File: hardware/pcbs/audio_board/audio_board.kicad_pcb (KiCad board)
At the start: 4 copper layers, 152 x 61.5 mm, 147 parts, among them J1 NC3FAH1, J10 DECT, J11 Conn_01x08, J2 NC3FAH1, J3 NC3FAH1, J4 NC3MAH, J5 NC3MAH, J6 AudioJack3, J7 Stereo Line-in, J8 I2C, Q1 2N7002, Q2 SI2309CDS-T1-GE3, Q3 2N7002, Q4 SI2309CDS-T1-GE3, Q5 2N7002, Q6 SI2309CDS-T1-GE3, Q7 S8050, U1 TAD5242, U2 TAD5242, U3 TAA3040, U5 LP5907MFX-3.3, U6 LM5158

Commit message: final touches to libraries
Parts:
- removed the U2 at (91.5, 120.5)
- added R7: 47, Resistor_SMD:R_0805_2012Metric, F.Cu at (174.2, 18.3)
- added R8: 47, Resistor_SMD:R_0805_2012Metric, F.Cu at (174.2, 21.2)
- added U5: TAD5242, ics:Texas_RGE0024R_VQFN-24-1EP_4x4mm_P0.5mm_EP2.1x2.1mm, F.Cu at (181.6, 28.3)
- J2: renamed from J11; footprint Library:mta100_01x8_P2.54_647050-8 -> Connector_MTA-100:mta100_01x8_P2.54_647050-8
- J3: renamed from J4; footprint Library:Jack_XLR_Neutrik_NC3MAH_Horizontal -> conn:Jack_XLR_Neutrik_NC3MAH_Horizontal
- J5: footprint Library:Jack_XLR_Neutrik_NC3MAH_Horizontal -> conn:Jack_XLR_Neutrik_NC3MAH_Horizontal
- J6: renamed from J1; footprint Library:Jack_XLR_Neutrik_NC3FAH2-LR-DAE_Horizontal -> conn:Jack_XLR_Neutrik_NC3FAH2-LR-DAE_Horizontal
- J7: renamed from J2; footprint Library:Jack_XLR_Neutrik_NC3FAH2-LR-DAE_Horizontal -> conn:Jack_XLR_Neutrik_NC3FAH2-LR-DAE_Horizontal
- J8: renamed from J3; footprint Library:Jack_XLR_Neutrik_NC3FAH2-LR-DAE_Horizontal -> conn:Jack_XLR_Neutrik_NC3FAH2-LR-DAE_Horizontal
- J9: renamed from J10; footprint Library:DectModule -> extra:DectModule
- U1: value TAD5242 -> ~; footprint Library:Texas_RGE0024R_VQFN-24-1EP_4x4mm_P0.5mm_EP2.1x2.1mm -> extra:Teensy41
- U3: value TAA3040 -> LM5158; footprint Package_DFN_QFN:WQFN-24-1EP_4x4mm_P0.5mm_EP2.6x2.6mm -> Package_DFN_QFN:WQFN-16-1EP_3x3mm_P0.5mm_EP1.68x1.68mm_ThermalVias
- U4: value ~ -> TAD5242; footprint Library:Teensy41 -> ics:Texas_RGE0024R_VQFN-24-1EP_4x4mm_P0.5mm_EP2.1x2.1mm
- U6: value LM5158 -> TAA3040; footprint Package_DFN_QFN:WQFN-16-1EP_3x3mm_P0.5mm_EP1.68x1.68mm_ThermalVias -> Package_DFN_QFN:WQFN-24-1EP_4x4mm_P0.5mm_EP2.6x2.6mm
- moved U6 127.5 mm to (181.9, 20.0)
- moved U1 112.0 mm to (163.1, 25.7), turned to 0 degrees
- moved U4 79.8 mm to (181.6, 36.6), turned to 0 degrees
- moved U3 69.4 mm to (181.4, 44.4)
- renumbered C29 to C1, C50 to C10, C51 to C11, C52 to C12, C9 to C13, C7 to C14, C11 to C15, C3 to C16, C1 to C17, C13 to C18, C5 to C19, C30 to C2, C2 to C20, C4 to C21, C6 to C22, C8 to C23, C10 to C24, C12 to C25, C14 to C26, C53 to C27, C15 to C28, C16 to C29, C37 to C3, C17 to C30, C18 to C31, C19 to C32, C20 to C33, C21 to C34, C22 to C35, C23 to C36, C24 to C37, C25 to C38, C26 to C39, C38 to C4, C27 to C40, C28 to C41, C31 to C42, C32 to C43, C33 to C44, C34 to C45, C35 to C46, C36 to C47, C41 to C48, C42 to C49, C39 to C5, C43 to C50, C44 to C51, C45 to C52, C46 to C53, C40 to C6, C47 to C7, C48 to C8, C49 to C9, D4 to D1, D5 to D2, D6 to D3, D1 to D4, D2 to D5, D3 to D6, H3 to H2, H2 to H3, J8 to J1, J7 to J10, J6 to J4, L7 to L1, L8 to L2, L9 to L3, L1 to L4, L2 to L5, L3 to L6, L4 to L7, L5 to L8, L6 to L9, Q7 to Q1, Q1 to Q2, Q2 to Q3, Q3 to Q4, Q4 to Q5, Q5 to Q6, Q6 to Q7, R11 to R1, R48 to R10, R49 to R11, R50 to R12, R51 to R13, R52 to R14, R1 to R15, R2 to R16, R3 to R17, R4 to R18, R5 to R19, R12 to R2, R7 to R20, R8 to R21, R9 to R22, R10 to R23, R15 to R24, R16 to R25, R17 to R26, R18 to R27, R19 to R28, R20 to R29, R13 to R3, R21 to R30, R22 to R31, R23 to R32, R24 to R33, R25 to R34, R26 to R35, R27 to R36, R29 to R37, R30 to R38, R31 to R39, R14 to R4, R32 to R40, R35 to R41, R36 to R42, R37 to R43, R38 to R44, R39 to R45, R40 to R46, R41 to R47, R42 to R48, R43 to R49, R71 to R5, R44 to R50, R45 to R51, R46 to R52, R6 to R53, R28 to R54, R72 to R6, R47 to R9, U5 to U2
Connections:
- C11 pad 1: Net-(U6-COMP) -> Net-(U3-COMP)
- C16 pad 1: Net-(U1-DREG) -> Net-(U4-DREG)
- C17 pad 1: Net-(U1-VREF) -> Net-(U4-VREF)
- C19 pad 1: Net-(U1-DREG) -> Net-(U4-DREG)
- C27 pad 1: Net-(U3-VREF) -> Net-(U6-VREF)
- C28 pad 1: Net-(U3-AREG) -> Net-(U6-AREG)
- C29 pad 1: Net-(U3-AREG) -> Net-(U6-AREG)
- C34 pad 1: Net-(U3-DREG) -> Net-(U6-DREG)
- C35 pad 1: Net-(U3-DREG) -> Net-(U6-DREG)
- C7 pad 1: Net-(U6-VCC) -> Net-(U3-VCC)
- C8 pad 1: Net-(U6-SS) -> Net-(U3-SS)
- J4 pad S: /HP_GND -> Net-(J4-PadS)
- R10 pad 2: Net-(U6-RT) -> Net-(U3-RT)
- R11 pad 2: Net-(U6-MODE) -> Net-(U3-MODE)
- R12 pad 1: Net-(U6-FB) -> Net-(U3-FB)
- R13 pad 2: Net-(U6-FB) -> Net-(U3-FB)
- R14 pad 2: Net-(U6-COMP) -> Net-(U3-COMP)
- R15 pad 1: Net-(U1-MD0) -> Net-(U4-MD0)
- U1 pad 1: Net-(U1-DREG) -> unconnected-(U1-Pad1)
- U1 pad 10: GND -> /CS_RIGHT
- U1 pad 11: unconnected-(U1-GPO-Pad11) -> /MOSI
- U1 pad 12: GND -> /DC
- U1 pad 13: Net-(U1-MD0) -> /SCK
- U1 pad 14: GND -> /DECT_TX
- U1 pad 15: GND -> /DECT_RX
- U1 pad 16: GND -> /SCL1
- U1 pad 17: GND -> /SDA1
- U1 pad 18: GND -> /SDA
- U1 pad 19: /DAC 1/OUTA- -> /SCL
- U1 pad 2: /I2S1_BCLK -> /I2S2_TX
- U1 pad 20: /DAC 1/OUTA+ -> /I2S1_LRCLK
- U1 pad 21: /DAC 1/OUTB+ -> /I2S1_BCLK
- U1 pad 22: /DAC 1/OUTB- -> unconnected-(U1-Pad22)
- U1 pad 23: +3.3VA -> /I2S1_MCLK
- U1 pad 24: Net-(U1-VREF) -> /RESET
- U1 pad 25: GND -> unconnected-(U1-Pad25)
- U1 pad 3: /I2S1_LRCLK -> /I2S2_FS
- U1 pad 4: /DAC 1/DOUT -> /I2S2_BCLK
- U1 pad 5: /I2S1_TX1 -> /I2S2_RX
- U1 pad 6: +3.3V -> /I2S1_RX2
- U1 pad 7: +3.3V -> /I2S1_TX1
- U1 pad 8: +3.3V -> /I2S1_RX1
- U1 pad 9: GND -> /CS_LEFT
- U3 pad 1: +3.3VA -> GND
- U3 pad 10: /ADC/IN3+ -> Net-(U3-SS)
- U3 pad 11: /ADC/IN3- -> Net-(U3-MODE)
- U3 pad 12: /ADC/IN4+ -> unconnected-(U3-NC-Pad12)
- U3 pad 13: GND -> /Power/SW
- U3 pad 14: +3.3V -> /Power/SW
- U3 pad 15: +3.3V -> unconnected-(U3-NC-Pad15)
- U3 pad 17: /SCL1 -> GND
- U3 pad 2: Net-(U3-AREG) -> Net-(U3-VCC)
- U3 pad 3: Net-(U3-VREF) -> +5V
- U3 pad 4: GND -> unconnected-(U3-PGOOD-Pad4)
- U3 pad 5: unconnected-(U3-MICBIAS-Pad5) -> Net-(U3-RT)
- U3 pad 6: /ADC/IN1+ -> +5V
- U3 pad 7: /ADC/IN1- -> GND
- U3 pad 8: /ADC/IN2+ -> Net-(U3-COMP)
- U3 pad 9: /ADC/IN2- -> Net-(U3-FB)
- U4 pad 1: unconnected-(U4-Pad1) -> Net-(U4-DREG)
- U4 pad 10: /CS_RIGHT -> GND
- U4 pad 11: /MOSI -> unconnected-(U4-GPO-Pad11)
- U4 pad 12: /DC -> GND
- U4 pad 13: /SCK -> Net-(U4-MD0)
- U4 pad 14: /DECT_TX -> GND
- U4 pad 15: /DECT_RX -> GND
- U4 pad 16: /SCL1 -> GND
- U4 pad 17: /SDA1 -> GND
- U4 pad 18: /SDA -> GND
- U4 pad 19: /SCL -> /DAC 1/OUTA-
- U4 pad 2: /I2S2_TX -> /I2S1_BCLK
- U4 pad 20: /I2S1_LRCLK -> /DAC 1/OUTA+
- U4 pad 21: /I2S1_BCLK -> /DAC 1/OUTB+
- U4 pad 22: unconnected-(U4-Pad22) -> /DAC 1/OUTB-
- U4 pad 23: /I2S1_MCLK -> +3.3VA
- U4 pad 24: /RESET -> Net-(U4-VREF)
- U4 pad 25: unconnected-(U4-Pad25) -> GND
- U4 pad 3: /I2S2_FS -> /I2S1_LRCLK
- U4 pad 4: /I2S2_BCLK -> /DAC 1/DOUT
- U4 pad 5: /I2S2_RX -> /I2S1_TX1
- U4 pad 6: /I2S1_RX2 -> +3.3V
- U4 pad 7: /I2S1_TX1 -> +3.3V
- U4 pad 8: /I2S1_RX1 -> +3.3V
- U4 pad 9: /CS_LEFT -> GND
- U6 pad 1: GND -> +3.3VA
- U6 pad 10: Net-(U6-SS) -> /ADC/IN3+
- U6 pad 11: Net-(U6-MODE) -> /ADC/IN3-
- U6 pad 12: unconnected-(U6-NC-Pad12) -> /ADC/IN4+
- U6 pad 13: /Power/SW -> GND
- U6 pad 14: /Power/SW -> +3.3V
- U6 pad 15: unconnected-(U6-NC-Pad15) -> +3.3V
- U6 pad 17: (no net) -> /SCL1
- U6 pad 2: Net-(U6-VCC) -> Net-(U6-AREG)
- U6 pad 3: +5V -> Net-(U6-VREF)
- U6 pad 4: unconnected-(U6-PGOOD-Pad4) -> GND
- U6 pad 5: Net-(U6-RT) -> unconnected-(U6-MICBIAS-Pad5)
- U6 pad 6: +5V -> /ADC/IN1+
- U6 pad 7: GND -> /ADC/IN1-
- U6 pad 8: Net-(U6-COMP) -> /ADC/IN2+
- U6 pad 9: Net-(U6-FB) -> /ADC/IN2-
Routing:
- net Net-(J4-PadS): track 0.00 -> 71.4 mm, vias 0 -> 3
- net /HP_GND: track 71.4 -> 0.00 mm, vias 3 -> 0
- net Net-(U4-DREG): track 0.00 -> 7.87 mm
- net Net-(U1-DREG): track 7.87 -> 0.00 mm
- net Net-(U6-FB): track 7.14 -> 0.00 mm
- net Net-(U3-FB): track 0.00 -> 7.14 mm
- net Net-(U6-VREF): track 0.00 -> 6.49 mm
- net Net-(U3-VREF): track 6.49 -> 0.00 mm
- net Net-(U6-DREG): track 0.00 -> 6.12 mm
- net Net-(U3-DREG): track 6.12 -> 0.00 mm
- net Net-(U6-AREG): track 0.00 -> 5.93 mm
- net Net-(U3-AREG): track 5.93 -> 0.00 mm
- net Net-(U6-RT): track 4.54 -> 0.00 mm
- net Net-(U3-RT): track 0.00 -> 4.54 mm
- net Net-(U6-COMP): track 4.40 -> 0.00 mm
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
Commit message: some placement
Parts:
- moved U3 112.5 mm to (86.0, 104.0)
- moved U1 81.1 mm to (136.1, 102.2), turned to 90 degrees
- moved J2 19.2 mm to (124.3, 95.9), turned to 180 degrees

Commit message: audio board
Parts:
- moved C12 7.92 mm to (76.2, 99.1)
- moved C10 4.95 mm to (79.3, 99.0)
- moved C11 4.95 mm to (79.8, 108.8)
- moved C5 4.95 mm to (74.8, 105.7)
- moved C6 4.95 mm to (76.8, 105.7)
- moved C7 4.95 mm to (76.8, 102.3)
- moved C8 4.95 mm to (86.5, 106.0)
- moved C9 4.95 mm to (80.8, 111.6)
- moved D3 4.95 mm to (82.8, 97.7)
- moved R12 4.95 mm to (88.5, 108.2)
- moved R14 4.95 mm to (81.8, 108.8)
- moved U3 4.95 mm to (81.1, 104.1)
- moved L2 4.95 mm to (87.2, 100.6)
- moved R10 4.95 mm to (76.2, 108.6)
- moved R11 4.95 mm to (86.5, 104.0)
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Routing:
- net /Power/48VREG: track 13.9 -> 16.5 mm

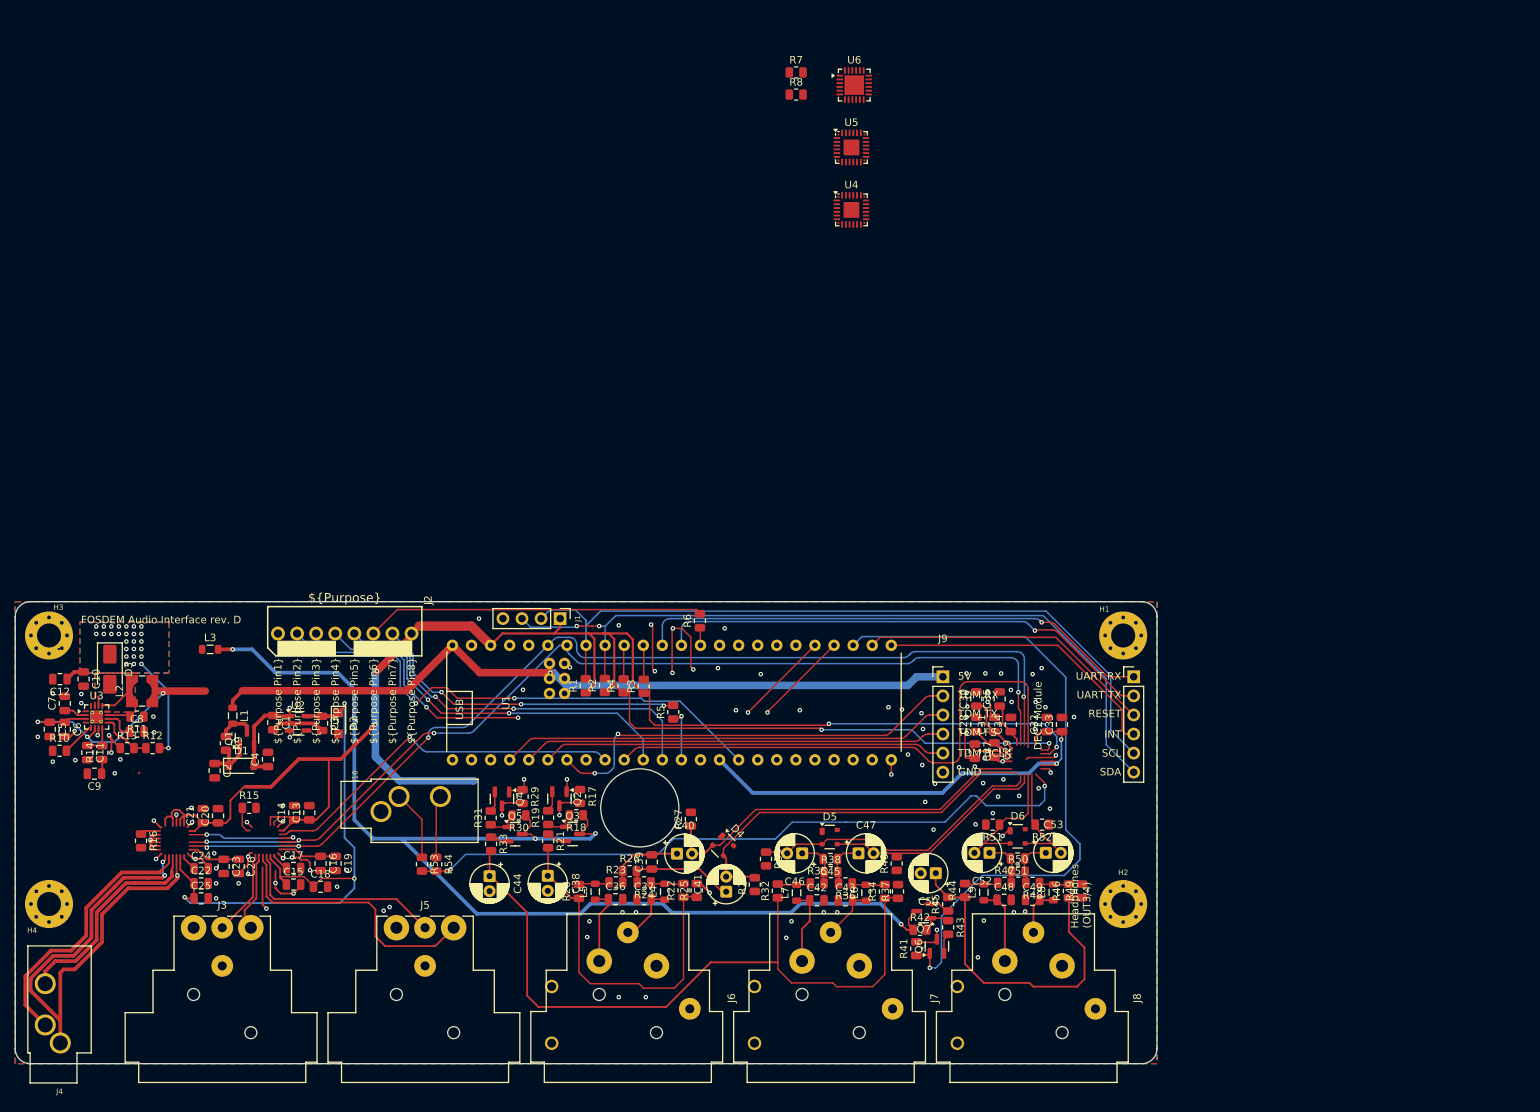
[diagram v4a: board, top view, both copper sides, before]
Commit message: add vias and mask to ic packages and route dac
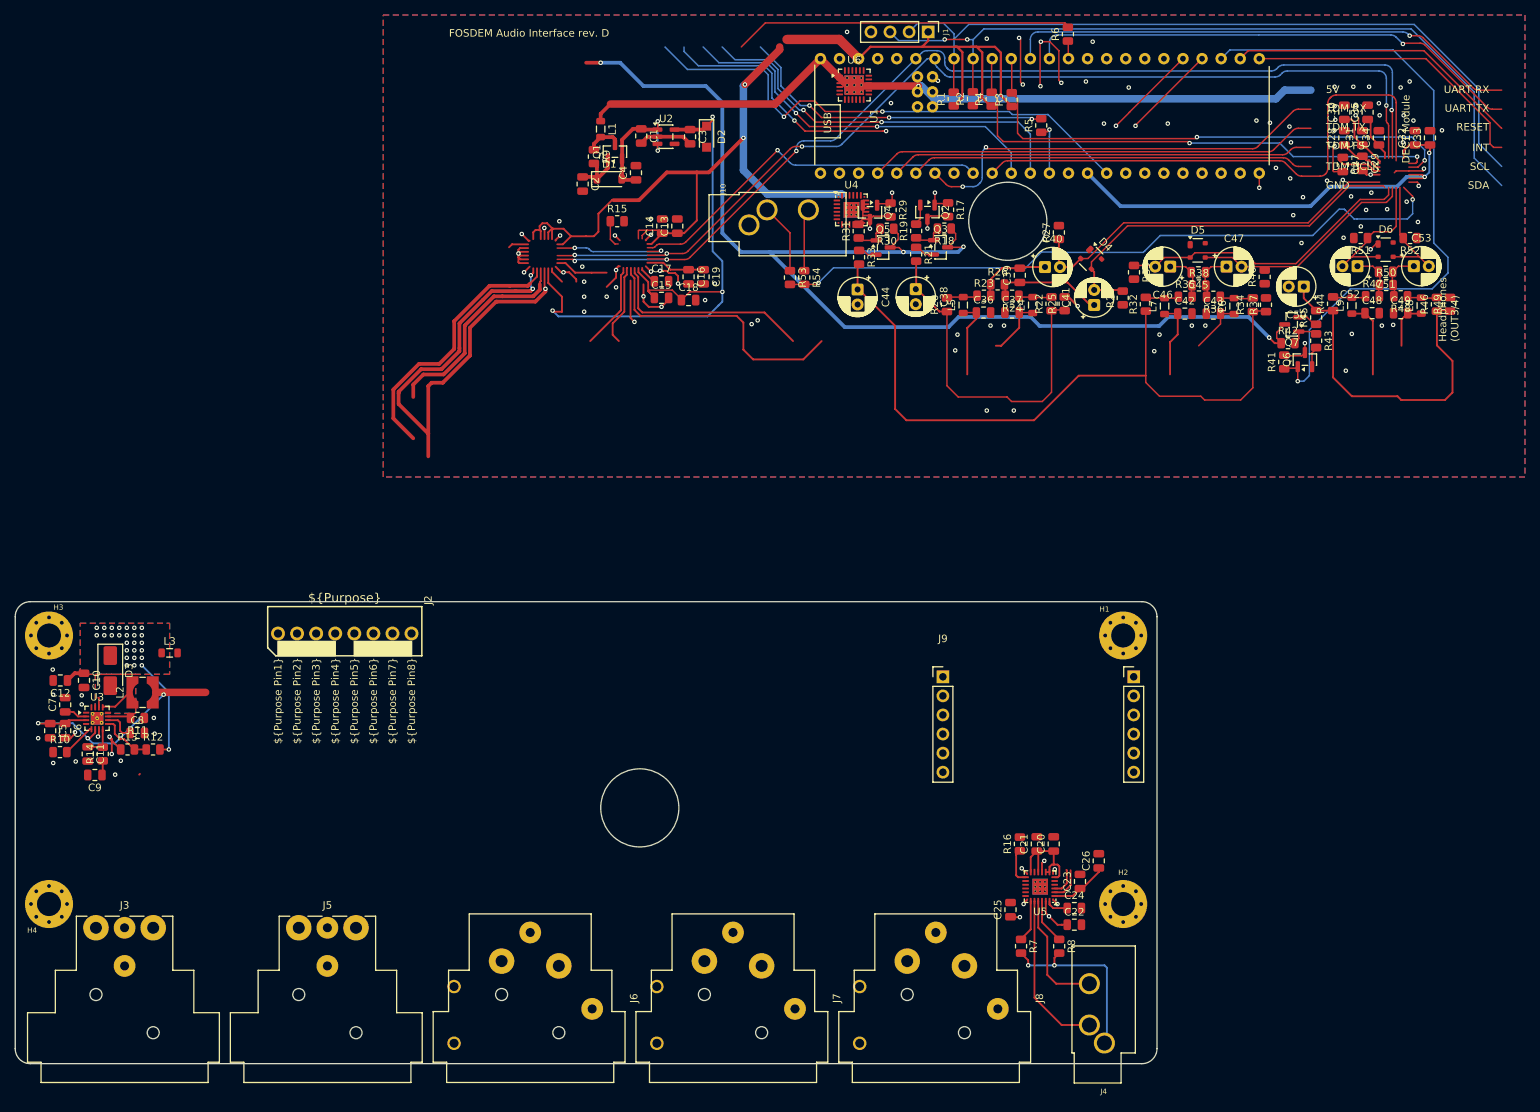
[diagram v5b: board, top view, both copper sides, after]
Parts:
- U3: footprint Package_DFN_QFN:WQFN-16-1EP_3x3mm_P0.5mm_EP1.68x1.68mm_ThermalVias -> ics:WQFN-16-1EP_3x3mm_P0.5mm_EP1.68x1.68mm_ThermalVias
- U6: footprint Package_DFN_QFN:WQFN-24-1EP_4x4mm_P0.5mm_EP2.6x2.6mm -> ics:WQFN-24-1EP_4x4mm_P0.5mm_EP2.6x2.6mm
- moved J4 139.0 mm to (215.2, 147.5)
- moved R7 120.1 mm to (204.2, 134.6), turned to -90 degrees
- moved R8 118.7 mm to (209.2, 134.6), turned to -90 degrees
- moved R16 117.0 mm to (204.0, 121.0), turned to 90 degrees
- moved C22 116.4 mm to (211.2, 131.8)
- moved C24 116.4 mm to (211.2, 129.5)
- moved C26 114.5 mm to (214.5, 123.2), turned to 90 degrees
- moved C23 114.0 mm to (212.0, 126.0), turned to 90 degrees
- moved C20 111.3 mm to (208.5, 121.0)
- moved C21 111.1 mm to (206.2, 121.0)
- moved C25 107.8 mm to (202.8, 129.8), turned to 90 degrees
- moved U5 101.6 mm to (206.7, 126.7), turned to 180 degrees
- moved C1 92.2 mm to (153.6, 26.8)
- moved C28 92.2 mm to (247.2, 27.0)
- moved C29 92.2 mm to (249.6, 30.4)
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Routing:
- net GND: track 106.0 -> 247.3 mm, vias 116 -> 124
- net Net-(J4-PadS): track 71.4 -> 24.7 mm, vias 3 -> 2
- net +3.3V: track 159.1 -> 174.0 mm
- net /HP_L: track 36.2 -> 21.7 mm
- net /HP_R: track 28.8 -> 16.4 mm
- net +3.3VA: track 88.3 -> 98.6 mm, vias 3 -> 5
- net Net-(U5-DREG): track 7.12 -> 14.9 mm
- net /HP_GND: track 0.00 -> 6.04 mm
- net /DAC 2/OUTA-: track 0.00 -> 5.62 mm
- net Net-(U5-MD0): track 2.70 -> 7.54 mm
- net /I2S1_BCLK: track 139.7 -> 144.2 mm
- net /I2S1_LRCLK: track 136.7 -> 140.4 mm
- net Net-(U5-VREF): track 2.34 -> 5.33 mm
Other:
- board size 152 x 61.5 mm -> 152 x 117.3 mm

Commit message: route one input
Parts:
- removed C38, C44: 10μF 100V, Capacitor_THT:CP_Radial_D5.0mm_P2.00mm
- removed Q2, Q4: 2N7002, Package_TO_SOT_SMD:SOT-23
- removed Q3, Q5: SI2309CDS-T1-GE3, Package_TO_SOT_SMD:SOT-23
- removed R17, R29: 10kΩ, Resistor_SMD:R_0805_2012Metric
- removed R18, R30: 22kΩ, Resistor_SMD:R_0805_2012Metric
- removed R19, R31: 100kΩ, Resistor_SMD:R_0805_2012Metric
- removed R21, R33: 470Ω, Resistor_SMD:R_0805_2012Metric
- moved C49 99.7 mm to (192.8, 128.5)
- moved C50 99.7 mm to (179.9, 125.0)
- moved C52 99.7 mm to (187.1, 122.2)
- moved C53 99.7 mm to (194.6, 122.2)
- moved L8 99.7 mm to (195.6, 127.5)
- moved L9 99.7 mm to (186.3, 127.5)
- moved Q6 99.7 mm to (180.1, 134.7)
- moved Q7 99.7 mm to (178.3, 130.0)
- moved R41 99.7 mm to (177.3, 135.0)
- moved R42 99.7 mm to (177.8, 132.5)
- moved R43 99.7 mm to (181.6, 132.2)
- moved R44 99.7 mm to (183.8, 127.2)
- moved R45 99.7 mm to (181.6, 129.1)
- moved R47 99.7 mm to (189.1, 126.2)
- moved R48 99.7 mm to (192.8, 126.2)
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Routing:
- net GND: track 247.3 -> 12.4 mm, vias 124 -> 20
- net +3.3V: track 174.0 -> 15.0 mm, vias 4 -> 0
- net +48V: track 160.2 -> 2.70 mm, vias 4 -> 0
- net /I2S1_BCLK: track 144.2 -> 4.51 mm, vias 4 -> 0
- net /I2S1_LRCLK: track 140.4 -> 3.72 mm, vias 4 -> 0
- net /SDA: track 103.3 -> 0.00 mm, vias 2 -> 0
- net +5V: track 137.9 -> 36.7 mm, vias 4 -> 3
- net /SCL: track 100.6 -> 0.00 mm
- net Net-(C44-Pad1): track 95.3 -> 0.00 mm
- net /ADC/IN4+: track 91.9 -> 0.00 mm, vias 2 -> 0
- net +3.3VA: track 98.6 -> 10.3 mm, vias 5 -> 2
- net /PHANTOM_IN3_EN: track 89.5 -> 1.92 mm, vias 1 -> 0
- net /I2S1_RX1: track 73.3 -> 0.00 mm
- net /PHANTOM_IN2_EN: track 72.5 -> 0.00 mm, vias 2 -> 0
- net /RESET: track 69.5 -> 0.00 mm, vias 2 -> 0
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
